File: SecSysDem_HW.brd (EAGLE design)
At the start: 99 x 80 mm, 47 parts, among them Q1 2N3904, T1 MOSFET_NCHANNEL_ENHANCEMENT2N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, T2 MOSFET_NCHANNEL_ENHANCEMENT2N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, T3 MOSFET_NCHANNEL_ENHANCEMENT2N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, U1 XPLAINED_MINI_PINOUT, U2 PCF8574_IO_EXPANDER, U4 FT24C512A, U5 MCP4901-E/SN, X1 C-GRID-06-70553, X5 C-GRID-02-70543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

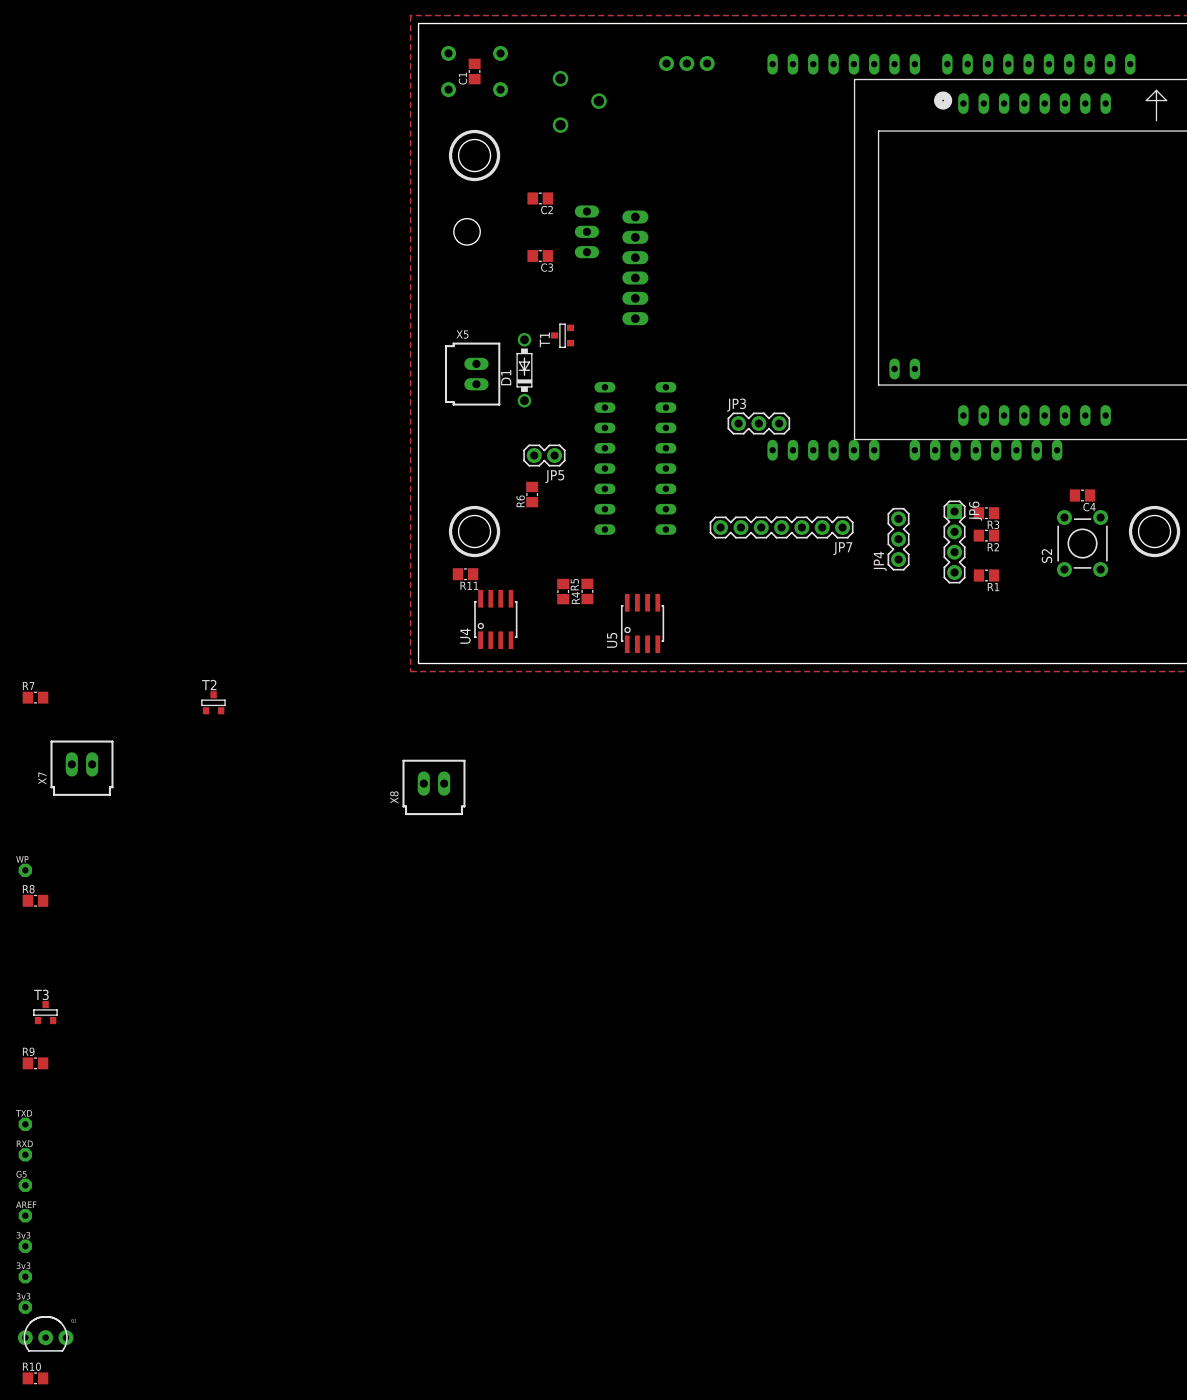
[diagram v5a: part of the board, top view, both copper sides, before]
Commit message: Continued board layout. Most components in proper place. No traces yet.
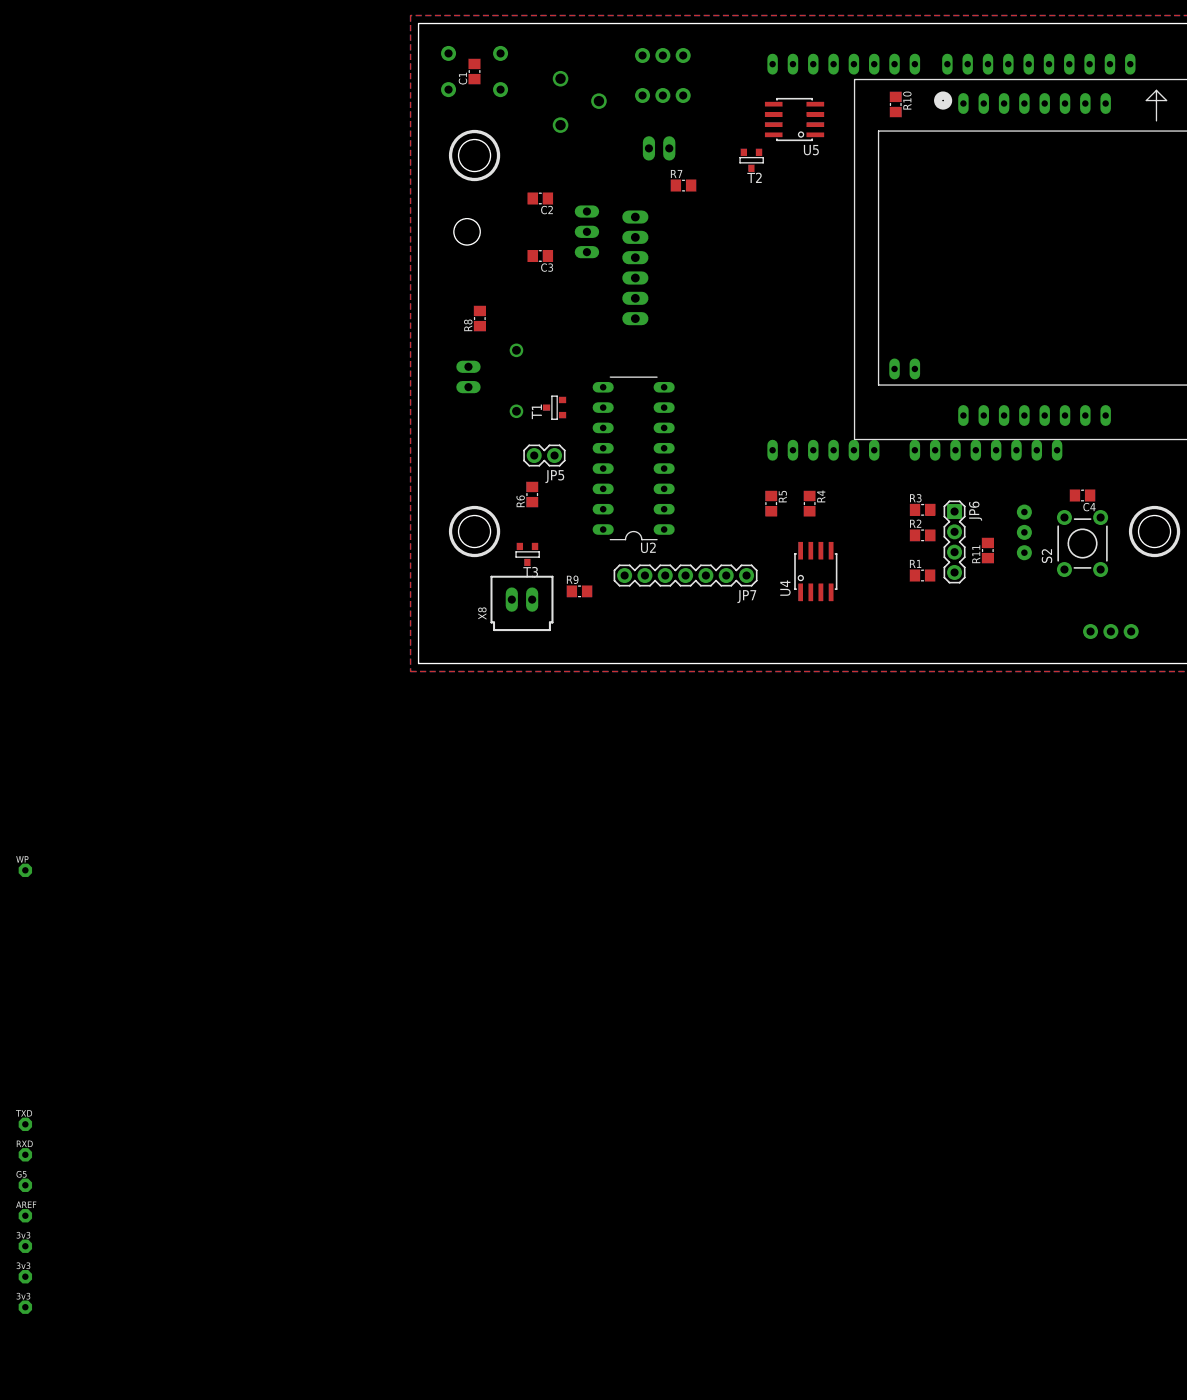
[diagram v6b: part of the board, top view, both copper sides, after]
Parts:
- moved R10 192.1 mm to (59.6, 58.9), turned to 270 degrees
- moved Q1 158.4 mm to (75.7, 5.39), flipped to the bottom, turned to 90 degrees
- moved X7 105.5 mm to (30.1, 53.4), flipped to the bottom
- moved R7 103.2 mm to (33.1, 48.7)
- moved T2 95.5 mm to (41.6, 51.9), turned to 180 degrees
- moved R8 91.6 mm to (7.66, 32.1), turned to 90 degrees
- moved R9 90.0 mm to (20.1, -1.98)
- moved T3 83.1 mm to (13.6, 2.63), turned to 180 degrees
- moved U5 65.8 mm to (47.0, 57.0), turned to 90 degrees
- moved R11 65.3 mm to (71.2, 3.12), turned to 90 degrees
- moved JP3 42.7 mm to (28.0, 60.0), flipped to the bottom, turned to 180 degrees
- moved U4 40.4 mm to (49.7, 0.50)
- moved R4 29.9 mm to (48.9, 8.99), turned to 270 degrees
- moved R5 28.2 mm to (44.1, 8.99)
- moved JP4 25.6 mm to (84.0, -7.00), flipped to the bottom, turned to 180 degrees
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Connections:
- net GND: now also U5.5

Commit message: Continued PCB layout.
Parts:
- moved T2 1.41 mm to (42.6, 50.9)
- moved R11 1.02 mm to (71.8, 3.88), turned to 270 degrees
- moved C4 1.00 mm to (82.0, 10.0)
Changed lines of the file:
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@@
 <element name="R5" library="Luke" package="C0805" value="10k" x="44.08" y="8.99" rot="R270"/>
 <element name="S2" library="Luke" package="TACTILE_SWITCH" value="TACTILE_SWITCHTHROUGH_HOLE" x="83" y="4" rot="R90"/>
-<element name="C4" library="Luke" package="C0805" value="1uF" x="83" y="10" rot="R180"/>
+<element name="C4" library="Luke" package="C0805" value="1uF" x="82" y="10" rot="R180"/>
 <element name="R6" library="Luke" package="C0805" value="2.2k" x="14.21" y="10.12" rot="R90"/>
-<element name="T2" library="Luke" package="SOT23" value="MOSFET_NCHANNEL_ENHANCEMENT2N7002,215" x="41.61" y="51.91" rot="R180">
-<attribute name="ID" value="300 mA" x="41.61" y="51.91" size="1.778" layer="27" rot="R180" display="off"/>
-<attribute name="VGS" value="2 V" x="41.61" y="51.91" size="1.778" layer="27" rot="R180" display="off"/>
-<attribute name="POWER" value="830 mW" x="41.61" y="51.91" size="1.778" layer="27" rot="R180" display="off"/>
-<attribute name="VDS" value="60 V" x="41.61" y="51.91" size="1.778" layer="27" rot="R180" display="off"/>
+<element name="T2" library="Luke" package="SOT23" value="MOSFET_NCHANNEL_ENHANCEMENT2N7002,215" x="42.61" y="50.91" rot="R180">
+<attribute name="ID" value="300 mA" x="42.61" y="50.91" size="1.778" layer="27" rot="R180" display="off"/>
+<attribute name="VGS" value="2 V" x="42.61" y="50.91" size="1.778" layer="27" rot="R180" display="off"/>
+<attribute name="POWER" value="830 mW" x="42.61" y="50.91" size="1.778" layer="27" rot="R180" display="off"/>
+<attribute name="VDS" value="60 V" x="42.61" y="50.91" size="1.778" layer="27" rot="R180" display="off"/>
 </element>
 <element name="R7" library="Luke" package="C0805" value="10R" x="33.12" y="48.74"/>
@@
 <element name="Q1" library="SparkFun-DiscreteSemi" package="TO-92-AMMO" value="2N3904" x="75.73" y="5.39" rot="MR90"/>
 <element name="R10" library="Luke" package="C0805" value="1k" x="59.65" y="58.88" rot="R270"/>
-<element name="R11" library="Luke" package="C0805" value="100" x="71.16" y="3.12" rot="R90"/>
+<element name="R11" library="Luke" package="C0805" value="100" x="71.84" y="3.88" rot="R270"/>
 <element name="D1" library="diode" package="DO41-7.6" value="1N5819-T" x="12.24" y="24.34" rot="MR270"/>
 <element name="JP2" library="SparkFun-Connectors" package="1X03" value="" x="28" y="65" rot="MR180"/>
@@
 <wire x1="47.755" y1="3.1" x2="48.89" y2="8.04" width="0" layer="19" extent="1-1"/>
 <wire x1="67" y1="2.92" x2="48.89" y2="8.04" width="0" layer="19" extent="1-1"/>
-<wire x1="71.16" y1="2.17" x2="67" y2="2.92" width="0" layer="19" extent="1-1"/>
-<wire x1="72.2" y1="15.66" x2="71.16" y2="2.17" width="0" layer="19" extent="1-1"/>
+<wire x1="71.84" y1="4.83" x2="67" y2="2.92" width="0" layer="19" extent="1-1"/>
+<wire x1="72.2" y1="15.66" x2="71.84" y2="4.83" width="0" layer="19" extent="1-1"/>
 <wire x1="80.81" y1="20" x2="72.2" y2="15.66" width="0" layer="19" extent="1-1"/>
 <wire x1="27.1" y1="34.65" x2="17" y2="15" width="0" layer="19" extent="1-1"/>
@@
 <contactref element="S2" pad="4" route="any" routetag="G$1.2"/>
 <contactref element="C4" pad="1"/>
-<wire x1="83.95" y1="10" x2="62.04" y2="63.92" width="0" layer="19" extent="1-1"/>
-<wire x1="85.2606" y1="7.2512" x2="83.95" y2="10" width="0" layer="19" extent="1-1"/>
+<wire x1="82.95" y1="10" x2="62.04" y2="63.92" width="0" layer="19" extent="1-1"/>
+<wire x1="85.2606" y1="7.2512" x2="82.95" y2="10" width="0" layer="19" extent="1-1"/>
 </signal>
 <signal name="KEYPAD_1">
@@
 <contactref element="T2" pad="1"/>
 <contactref element="U5" pad="8"/>
-<wire x1="42.56" y1="52.91" x2="44.4" y2="55.095" width="0" layer="19" extent="1-1"/>
+<wire x1="43.56" y1="51.91" x2="44.4" y2="55.095" width="0" layer="19" extent="1-1"/>
 </signal>
 <signal name="N$8">
@@
 <contactref element="X7" pad="1"/>
 <contactref element="T2" pad="3"/>
-<wire x1="31.34" y1="53.39" x2="41.61" y2="50.91" width="0" layer="19" extent="1-1"/>
+<wire x1="31.34" y1="53.39" x2="42.61" y2="49.91" width="0" layer="19" extent="1-1"/>
 </signal>
 <signal name="N$7">
@@
 <contactref element="Q1" pad="1"/>
 <contactref element="R11" pad="2"/>
-<wire x1="71.16" y1="4.07" x2="75.73" y2="2.85" width="0" layer="19" extent="1-1"/>
+<wire x1="71.84" y1="2.93" x2="75.73" y2="2.85" width="0" layer="19" extent="1-1"/>
 </signal>
 <signal name="N$19">
